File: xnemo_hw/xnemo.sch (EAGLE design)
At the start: 36 parts, among them J1 MICRO_USB_B_RECEPT, J2 DM3D_MICRO_SD, J3 HEADER_2X5_0.05_SMD, J4 HEADER_2X5_0.05_THRU, J5 HEADER_2X5_0.05_THRU, U1 LTC3559, U2 L3GD20, U3 STM32F405RG, U5 HMC5883L, U6 ADXL345, X1 TXC_7A_XTAL

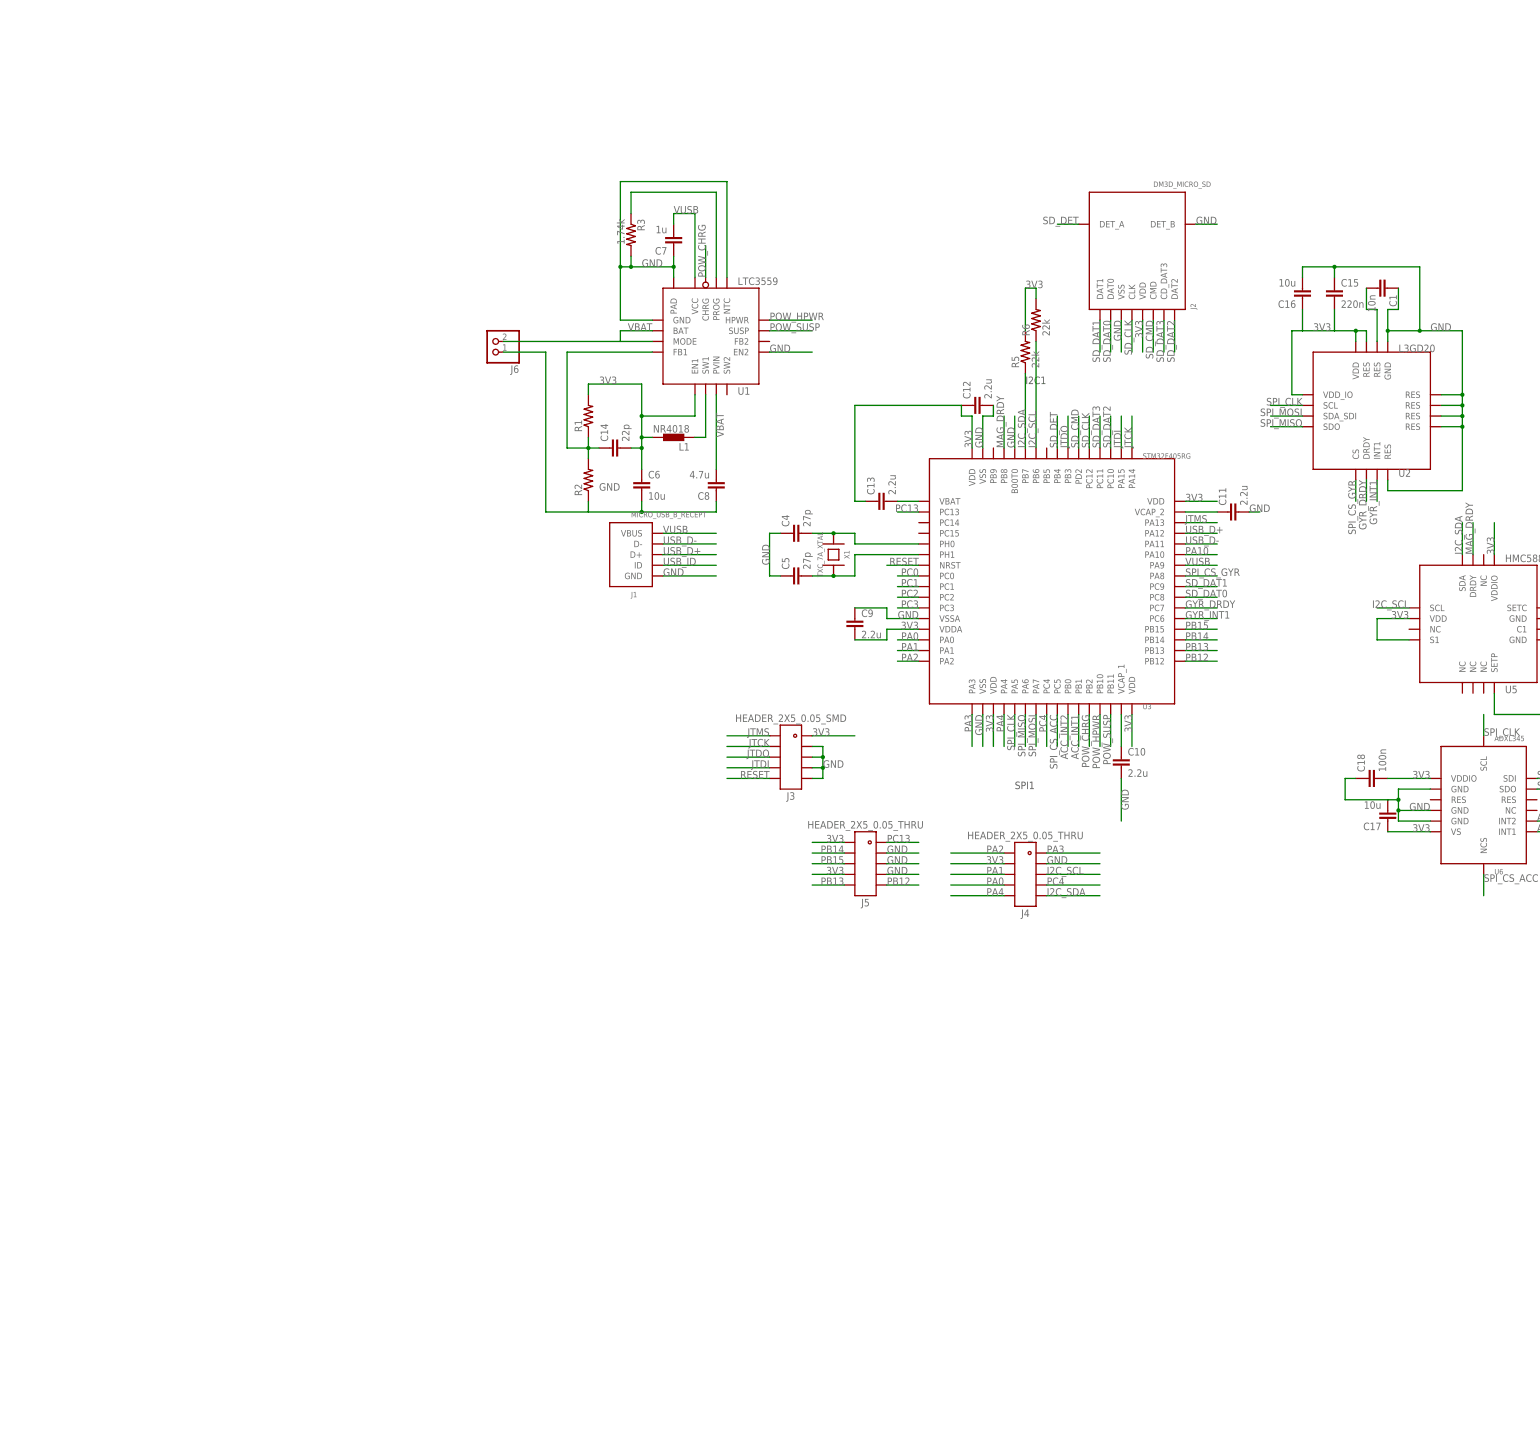
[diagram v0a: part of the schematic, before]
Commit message: Started conversion to larger PCB using LQFP100
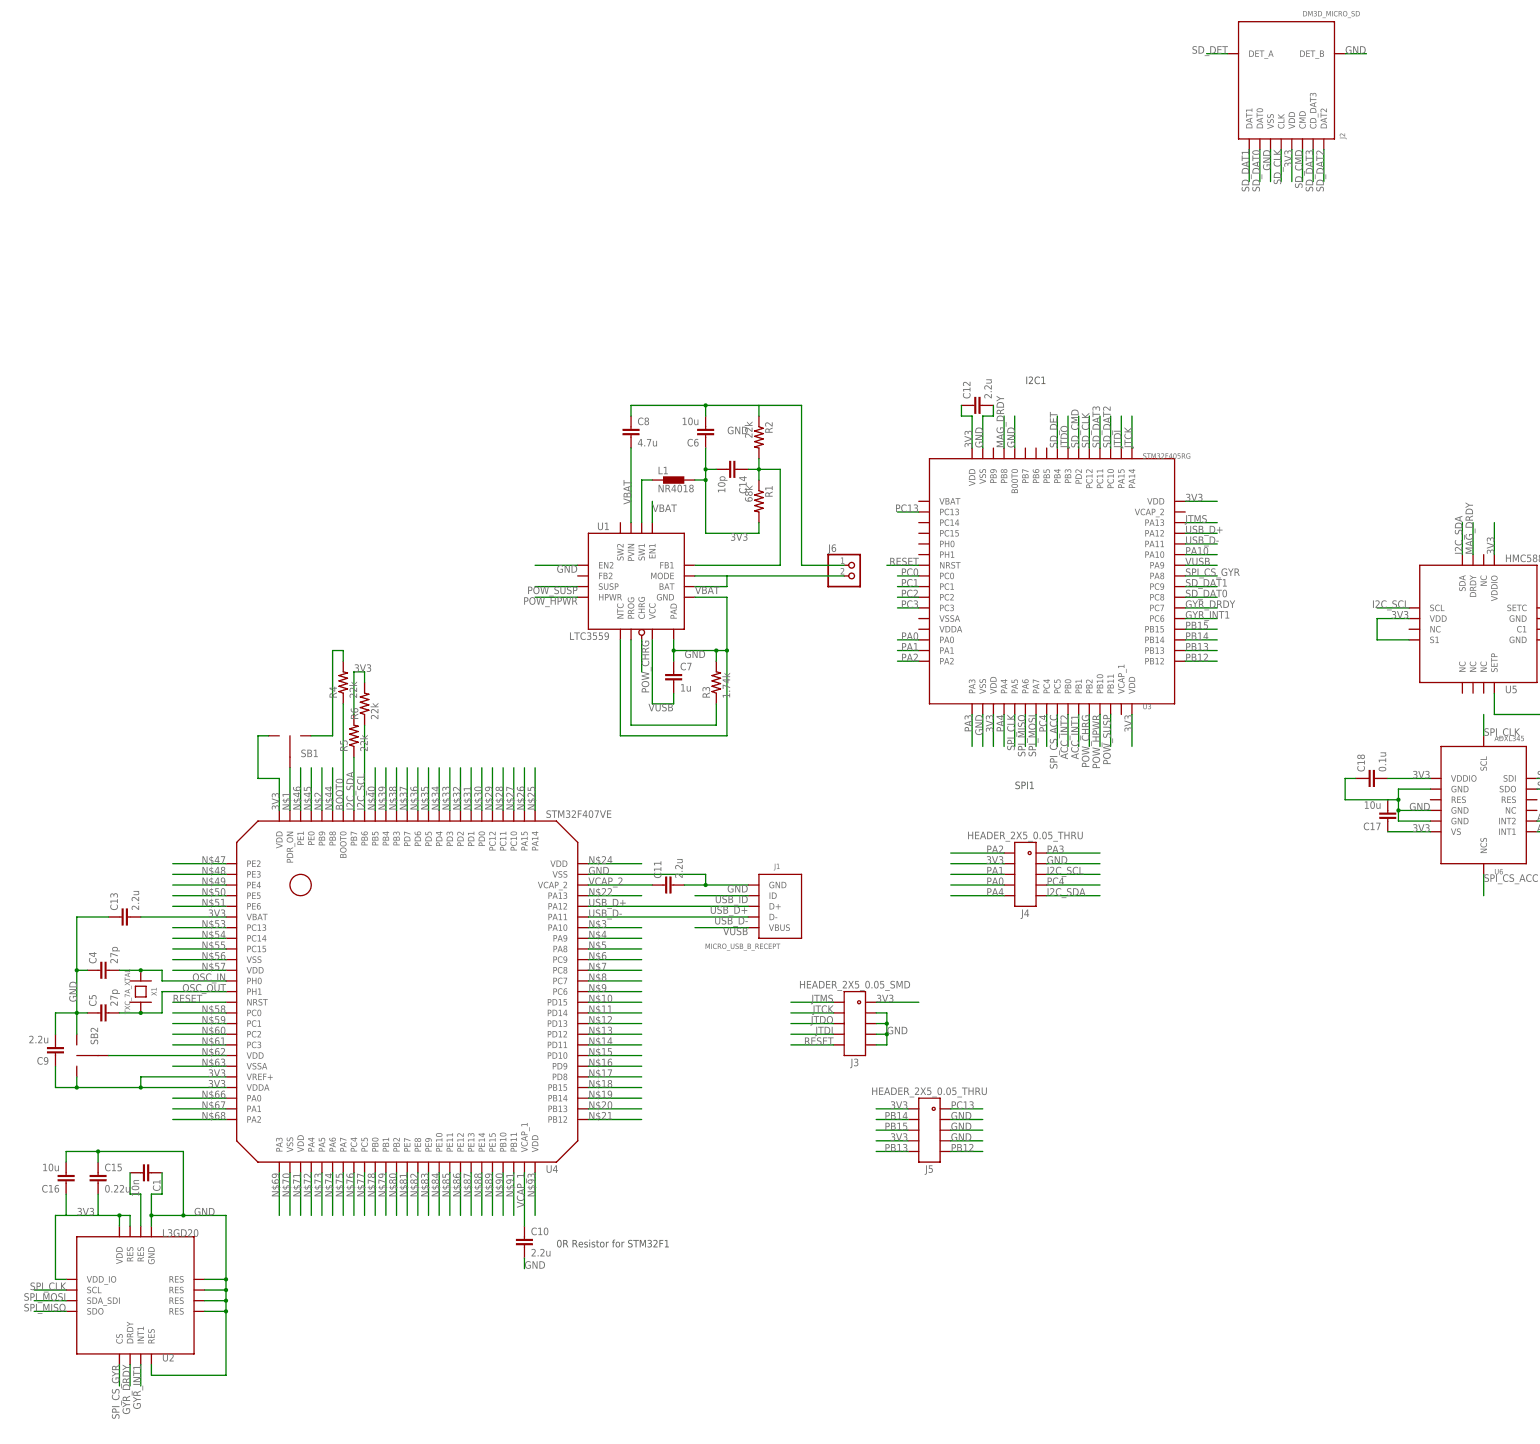
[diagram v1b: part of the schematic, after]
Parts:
- added R4: 22k, resistor:R-US_R0402
- added SB1, SB2: SOLDER_BRIDGE_2, xnemo:SOLDER_BRIDGE_2
- added U4: STM32F407VE, xnemo:STM32F407VE
- C14: value 22p -> 10p
- C15: value 220n -> 0.22u
- C18: value 100n -> 0.1u
- R1: value (none) -> 68k
- R2: value (none) -> 22k
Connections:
- removed net UC_VBAT: C13.2, U3.VBAT
- new net BOOT0: R4.1, U4.BOOT0
- new net N$1: SB1.P$3, U4.PDR_ON
- new net N$10: U4.PD15
- new net N$11: U4.PD14
- new net N$12: U4.PD13
- new net N$13: U4.PD12
- new net N$14: U4.PD11
- new net N$15: U4.PD10
- new net N$16: U4.PD9
- new net N$17: U4.PD8
- new net N$18: U4.PB15
- new net N$19: U4.PB14
- new net N$2: U4.PB9
- new net N$20: U4.PB13
- new net N$21: U4.PB12
- new net N$22: U4.PA13
- new net N$24: U4.VDD@5
- new net N$25: U4.PA14
- new net N$26: U4.PA15
- new net N$27: U4.PC10
- new net N$28: U4.PC11
- new net N$29: U4.PC12
- new net N$3: U4.PA10
- new net N$30: U4.PD0
- new net N$31: U4.PD1
- new net N$32: U4.PD2
- new net N$33: U4.PD3
- new net N$34: U4.PD4
- new net N$35: U4.PD5
- new net N$36: U4.PD6
- new net N$37: U4.PD7
- new net N$38: U4.PB3
- new net N$39: U4.PB4
- new net N$4: U4.PA9
- new net N$40: U4.PB5
- new net N$44: U4.PB8
- new net N$45: U4.PE0
- new net N$46: U4.PE1
- new net N$47: U4.PE2
- new net N$48: U4.PE3
- new net N$49: U4.PE4
- new net N$5: U4.PA8
- new net N$50: U4.PE5
- new net N$51: U4.PE6
- new net N$53: U4.PC13
- new net N$54: U4.PC14
- new net N$55: U4.PC15
- new net N$56: U4.VSS@1
- new net N$57: U4.VDD@1
- new net N$58: U4.PC0
- new net N$59: U4.PC1
- new net N$6: U4.PC9
- new net N$60: U4.PC2
- new net N$61: U4.PC3
- new net N$62: SB2.P$3, U4.VDD@2
- new net N$63: U4.VSSA
- new net N$66: U4.PA0
- new net N$67: U4.PA1
- new net N$68: U4.PA2
- new net N$69: U4.PA3
- new net N$7: U4.PC8
- new net N$70: U4.VSS@2
- new net N$71: U4.VDD@3
- new net N$72: U4.PA4
- new net N$73: U4.PA5
- new net N$74: U4.PA6
- new net N$75: U4.PA7
- new net N$76: U4.PC4
- new net N$77: U4.PC5
- new net N$78: U4.PB0
- new net N$79: U4.PB1
- new net N$8: U4.PC7
- new net N$80: U4.PB2
- new net N$81: U4.PE7
- new net N$82: U4.PE8
- new net N$83: U4.PE9
- new net N$84: U4.PE10
- new net N$85: U4.PE11
- new net N$86: U4.PE12
- new net N$87: U4.PE13
- new net N$88: U4.PE14
- new net N$89: U4.PE15
- new net N$9: U4.PC6
- new net N$90: U4.PB10
- new net N$91: U4.PB11
- new net N$93: U4.VDD@4
- net 3V3: now also C13.2, C9.1, SB1.P$1, SB2.P$1, U4.VBAT, U4.VDD@6, U4.VDDA, U4.VREF+; no longer C13.1, C9.2, U1.EN1, U3.VDDA
- net GND: now also C13.1, C9.2, R4.2, SB1.P$2, SB2.P$2, U4.VSS@3; no longer C9.1, U3.VSSA
- net I2C_SCL: now also U4.PB6; no longer U3.PB6
- net I2C_SDA: now also U4.PB7; no longer U3.PB7
- net OSC_IN: now also U4.PH0; no longer U3.PH0
- net OSC_OUT: now also U4.PH1; no longer U3.PH1
- net RESET: now also U4.NRST
- net USB_D+: now also U4.PA12
- net USB_D-: now also U4.PA11
- net VBAT: now also U1.EN1
- net VCAP_1: now also U4.VCAP_1; no longer U3.VCAP_1
- net VCAP_2: now also U4.VCAP_2; no longer U3.VCAP_2
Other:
- note added: "0R Resistor for STM32F1"
- moved on the sheet: C1, C10, C11, C13, C14, C15, C16, C4, C5, C6, C7, C8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
